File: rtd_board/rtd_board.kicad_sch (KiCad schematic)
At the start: 13 parts

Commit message: cleaning up
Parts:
- removed J?: Conn_02x18_Odd_Even, symbol Connector_Generic:Conn_02x18_Odd_Even
- removed J? (x2): Conn_01x15, symbol Connector_Generic:Conn_01x15
- removed U? (x9): MAX31865, symbol MAX31865:MAX31865
- removed U?: TCA9548A_Breakout, symbol TCA9548A_Breakout:TCA9548A_Breakout
- added J?: DSUB2, symbol Connector:DB15_Female
- added J?: DSUB3, symbol Connector:DB15_Female
- added J?: DSUB1, symbol Connector:DB15_Female
- added J?: Conn_02x18_Odd_Even, symbol Connector_Generic:Conn_02x18_Odd_Even
- added U? (x9): MAX31865, symbol MAX31865:MAX31865
- added U?: TCA9548A_Breakout, symbol TCA9548A_Breakout:TCA9548A_Breakout
- added U?: PCF8575_Breakout, symbol PCF8575_Breakout:PCF8575_Breakout
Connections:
- net +3V3: now also J?.1, J?.10 (P10), J?.12 (Pin_12), J?.4, U?. (VIN), U?.1 (V_IN), U?.1 (V_IN), U?.1 (V_IN), U?.1 (V_IN), U?.1 (V_IN), U?.1 (V_IN), U?.1 (V_IN), U?.1 (V_IN), U?.1 (V_IN)
- net FM1_INPT: now also J?.9 (P9)
- net FM2_INPT: now also J?.3
- net FM3_INPT: now also J?.12 (P12)
- net GND: now also J?.11 (P111), J?.2, J?.36 (Pin_36), J?.5, U?. (VIN), U?.7 (GND), U?.7 (GND), U?.7 (GND), U?.7 (GND), U?.7 (GND), U?.7 (GND), U?.7 (GND), U?.7 (GND), U?.7 (GND)
- net RTD1_CS: now also U?.5 (CS)
- net RTD1_SCK: now also U?.2 (SCK)
- net RTD1_SDI: now also U?.4 (SDI)
- net RTD1_SDO: now also U?.3 (SDO)
- new net MUX_SCL: J?.5 (Pin_5), U?. (VIN)
- new net MUX_SDA: J?.1 (Pin_1), U?. (VIN)
- new net RTD1_F+: J?.6, U?.9 (F+)
- new net RTD1_RTD+: J?.13 (P13), U?.11 (RTD+)
- new net RTD1_RTD-: J?.14 (P14), U?.12 (RTD-)
- new net RTD2_CS: U?.5 (CS)
- new net RTD2_F+: J?.15 (P15), U?.9 (F+)
- new net RTD2_RTD+: J?.7, U?.11 (RTD+)
- new net RTD2_RTD-: J?.8, U?.12 (RTD-)
- new net RTD2_SCK: U?.2 (SCK)
- new net RTD2_SDI: U?.4 (SDI)
- new net RTD3_CS: U?.5 (CS)
- new net RTD3_F+: J?.9 (P9), U?.9 (F+)
- new net RTD3_RTD+: J?.1, U?.11 (RTD+)
- new net RTD3_RTD-: J?.2, U?.12 (RTD-)
- new net RTD3_SCK: U?.2 (SCK)
- new net RTD3_SDI: U?.4 (SDI)
- new net RTD4_CS: U?.5 (CS)
- new net RTD4_F+: J?.3, U?.9 (F+)
- new net RTD4_RTD+: J?.10 (P10), U?.11 (RTD+)
- new net RTD4_RTD-: J?.11 (P111), U?.12 (RTD-)
- new net RTD4_SCK: U?.2 (SCK)
- new net RTD4_SDI: U?.4 (SDI)
- new net RTD4_SDO: U?.3 (SDO)
- new net RTD5_CS: U?.5 (CS)
- new net RTD5_F+: J?.12 (P12), U?.9 (F+)
- new net RTD5_RTD+: J?.4, U?.11 (RTD+)
- new net RTD5_RTD-: J?.14 (P14), J?.5, U?.12 (RTD-)
- new net RTD5_SCK: U?.2 (SCK)
- new net RTD5_SDI: U?.4 (SDI)
- new net RTD6_CS: U?.5 (CS)
- new net RTD6_F+: J?.6, U?.9 (F+)
- new net RTD6_RTD+: J?.13 (P13), U?.11 (RTD+)
- new net RTD6_RTD-: U?.12 (RTD-)
- new net RTD6_SCK: U?.2 (SCK)
- new net RTD6_SDI: U?.4 (SDI)
- new net RTD7_CS: U?.5 (CS)
- new net RTD7_F+: J?.15 (P15), U?.9 (F+)
- new net RTD7_RTD+: J?.7, U?.11 (RTD+)
- new net RTD7_RTD-: J?.8, U?.12 (RTD-)
- new net RTD7_SCK: U?.2 (SCK)
- new net RTD7_SDI: U?.4 (SDI)
- new net RTD7_SDO: U?.3 (SDO)
- new net RTD8_CS: U?.5 (CS)
- new net RTD8_F+: J?.9 (P9), U?.9 (F+)
- new net RTD8_RTD+: J?.1, U?.11 (RTD+)
- new net RTD8_RTD-: J?.2, U?.12 (RTD-), U?.12 (RTD-)
- new net RTD8_SCK: U?.2 (SCK)
- new net RTD8_SDI: U?.4 (SDI)
- new net RTD9_CS: U?.5 (CS)
- new net RTD9_F+: J?.3, U?.9 (F+)
- new net RTD9_RTD+: J?.10 (P10), U?.11 (RTD+)
- new net RTD9_RTD-: J?.11 (P111)
- new net RTD9_SCK: U?.2 (SCK)
- new net RTD9_SDI: U?.4 (SDI)
- no-connect marks 18 -> 27
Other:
- note added: "Address: 0x71"
- note added: "RTD 1"
- note added: "RTD 2"
- note added: "RTD 3"
- note added: "RTD 4"
- note added: "RTD 5"
- note added: "RTD 6"
- note added: "RTD 7"
- note added: "RTD 8"
- note added: "RTD 9"

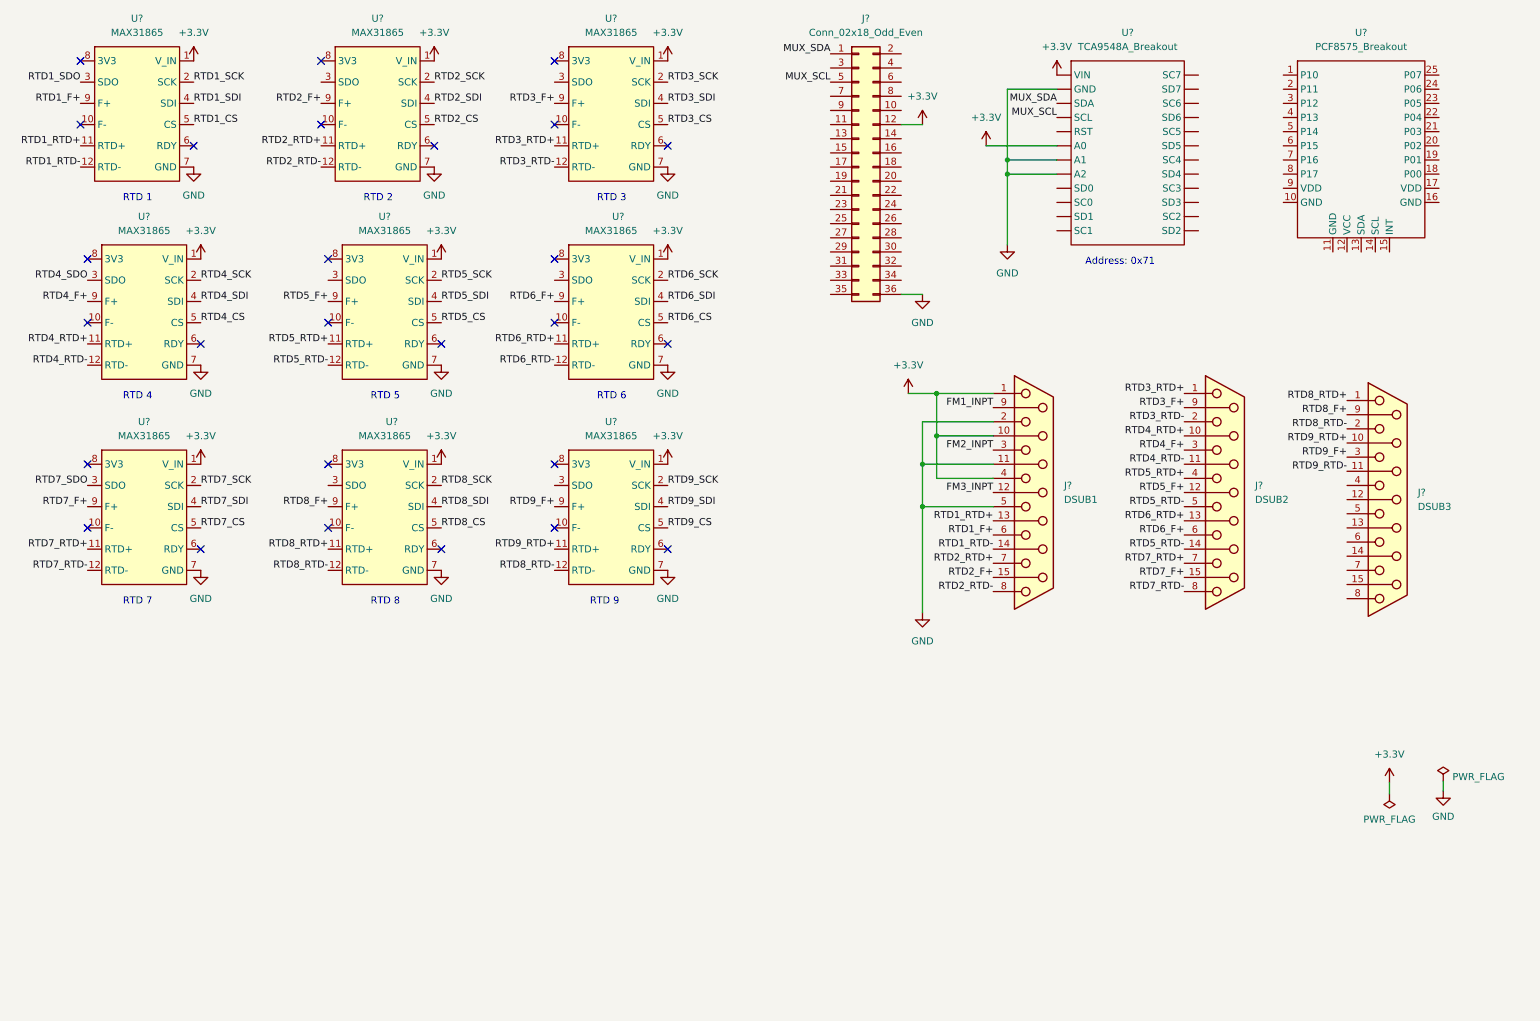
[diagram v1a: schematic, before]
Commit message: added screw terminals
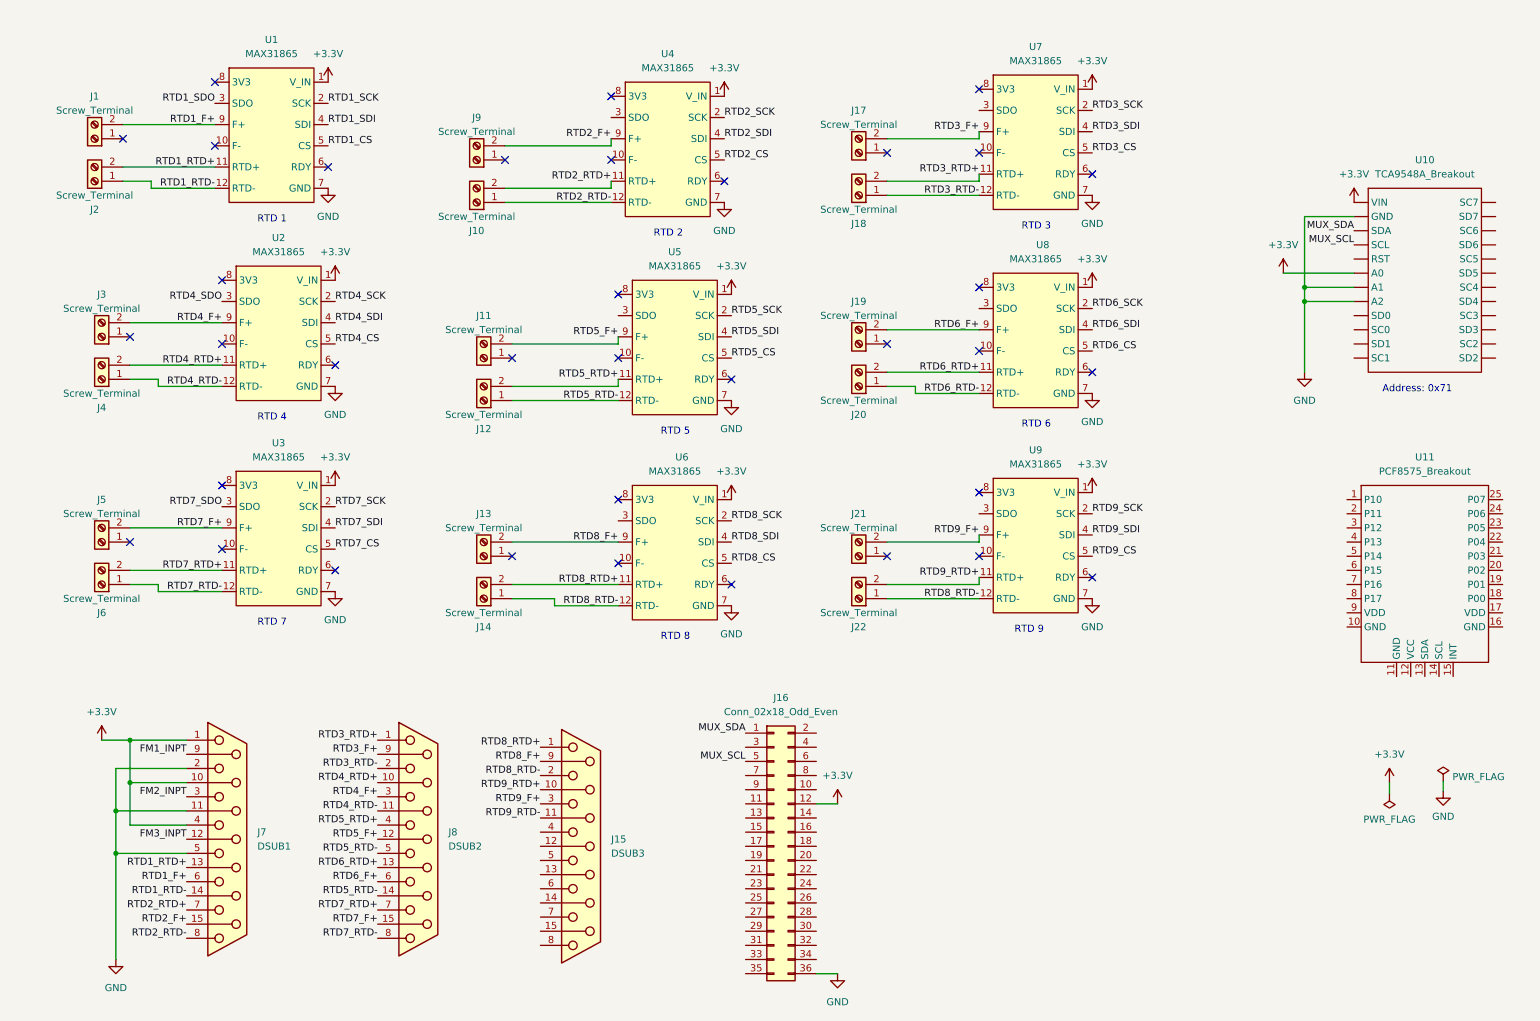
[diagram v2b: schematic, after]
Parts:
- added J1, J10, J11, J12, J13, J14, J17, J18, J19, J2, J20, J21, J22, J3, J4, J5, J6, J9: Screw_Terminal, symbol Connector:Screw_Terminal_01x02
- gave numbers to parts that had none: 15
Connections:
- net RTD1_F+: now also J1.2 (Pin_2)
- net RTD1_RTD+: now also J2.2 (Pin_2)
- net RTD1_RTD-: now also J2.1 (Pin_1)
- net RTD2_F+: now also J9.2 (Pin_2)
- net RTD2_RTD+: now also J10.2 (Pin_2)
- net RTD2_RTD-: now also J10.1 (Pin_1)
- net RTD3_F+: now also J17.2 (Pin_2)
- net RTD3_RTD+: now also J18.2 (Pin_2)
- net RTD3_RTD-: now also J18.1 (Pin_1)
- net RTD4_F+: now also J3.2 (Pin_2)
- net RTD4_RTD+: now also J4.2 (Pin_2)
- net RTD4_RTD-: now also J4.1 (Pin_1)
- net RTD5_F+: now also J11.2 (Pin_2)
- net RTD5_RTD+: now also J12.2 (Pin_2)
- net RTD5_RTD-: now also J12.1 (Pin_1)
- net RTD6_F+: now also J19.2 (Pin_2)
- net RTD6_RTD+: now also J20.2 (Pin_2)
- net RTD6_RTD-: now also J20.1 (Pin_1)
- net RTD7_F+: now also J5.2 (Pin_2)
- net RTD7_RTD+: now also J6.2 (Pin_2)
- net RTD7_RTD-: now also J6.1 (Pin_1)
- net RTD8_F+: now also J13.2 (Pin_2)
- net RTD8_RTD+: now also J14.2 (Pin_2)
- net RTD8_RTD-: now also J14.1 (Pin_1), J22.1 (Pin_1)
- net RTD9_F+: now also J21.2 (Pin_2)
- net RTD9_RTD+: now also J22.2 (Pin_2)
- no-connect marks 27 -> 36
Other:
- moved on the sheet: J15, J16, J7, J8, U1, U10, U11, U2, U3, U4, U5, U6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

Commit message: updates to layout + board settings, not complete yet
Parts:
- removed J1, J10, J11, J12, J13, J14, J17, J18, J19, J2, J20, J21, J22, J3, J4, J5, J6, J9: Screw_Terminal, symbol Connector:Screw_Terminal_01x02
- removed J15: DSUB3, symbol Connector:DB15_Female
- removed J16: Conn_02x18_Odd_Even, symbol Connector_Generic:Conn_02x18_Odd_Even
- removed U10: TCA9548A_Breakout, symbol TCA9548A_Breakout:TCA9548A_Breakout
- removed U11: PCF8575_Breakout, symbol PCF8575_Breakout:PCF8575_Breakout
- removed U9: MAX31865, symbol MAX31865:MAX31865
- added J1: PCIE-LP-01-01-F-DV-A-TR, Connector_PCBEdge:BUS_PCIexpress_x1, symbol PCIE-LP-01-01-F-DV-A-TR:PCIE-LP-01-01-F-DV-A-TR
- added U10: PCF8575_Breakout, PCF8575_Breakout:PCF8575_Breakout, symbol PCF8575_Breakout:PCF8575_Breakout
- J7, J8: footprint (none) -> DSUB_622-015-260-042:DSUB_622-015-260-042
- U1, U2, U3, U4, U5, U6, U7, U8: footprint (none) -> MAX31865_Breakout:MAX31865_Breakout
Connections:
- net FM1_INPT is gone; now on net RTD1_F+: J7.9 (P9)
- net FM2_INPT is gone; now on net RTD2_F+: J7.3
- net FM3_INPT is gone; now on net RTD3_F+: J7.12 (P12)
- net RTD1_SDO is gone; now on net SPI_MISO: U1.3 (SDO)
- net RTD2_SCK is gone; now on net SPI_SCK: U4.2 (SCK)
- net RTD2_SDI is gone; now on net SPI_MOSI: U4.4 (SDI)
- net RTD3_SCK is gone; now on net SPI_SCK: U7.2 (SCK)
- net RTD3_SDI is gone; now on net SPI_MOSI: U7.4 (SDI)
- net RTD4_SCK is gone; now on net SPI_SCK: U2.2 (SCK)
- net RTD4_SDI is gone; now on net SPI_MOSI: U2.4 (SDI)
- net RTD4_SDO is gone; now on net SPI_MISO: U2.3 (SDO)
- net RTD5_SCK is gone; now on net SPI_SCK: U5.2 (SCK)
- net RTD5_SDI is gone; now on net SPI_MOSI: U5.4 (SDI)
- net RTD6_SCK is gone; now on net SPI_SCK: U8.2 (SCK)
- net RTD6_SDI is gone; now on net SPI_MOSI: U8.4 (SDI)
- net RTD7_SCK is gone; now on net SPI_SCK: U3.2 (SCK)
- net RTD7_SDI is gone; now on net SPI_MOSI: U3.4 (SDI)
- net RTD7_SDO is gone; now on net SPI_MISO: U3.3 (SDO)
- net RTD8_SCK is gone; now on net SPI_SCK: U6.2 (SCK)
- net RTD8_SDI is gone; now on net SPI_MOSI: U6.4 (SDI)
- net GND: now also J1.A14, J1.A15, J1.B14, J1.B15, J1.B18, U10.10 (GND), U10.11 (GND), U10.16 (GND); no longer J7.11 (P111), J7.2, J7.5
- net RTD1_CS: now also U10.1 (P10)
- net RTD1_F+: no longer J7.6
- net RTD1_RTD+: now also J7.1; no longer J7.13 (P13)
- net RTD1_RTD-: now also J7.2; no longer J7.14 (P14)
- net RTD2_CS: now also U10.2 (P11)
- net RTD2_F+: no longer J7.15 (P15)
- net RTD2_RTD+: now also J7.10 (P10); no longer J7.7
- net RTD2_RTD-: now also J7.11 (P111); no longer J7.8
- net RTD3_CS: now also U10.3 (P12)
- net RTD3_F+: no longer J8.9 (P9)
- net RTD3_RTD+: now also J7.4; no longer J8.1
- net RTD3_RTD-: now also J7.5; no longer J8.2
- net RTD4_CS: now also U10.4 (P13)
- net RTD4_F+: now also J7.6; no longer J8.3
- net RTD4_RTD+: now also J7.13 (P13); no longer J8.10 (P10)
- net RTD4_RTD-: now also J7.14 (P14); no longer J8.11 (P111)
- net RTD5_CS: now also U10.5 (P14)
- net RTD5_F+: now also J7.15 (P15); no longer J8.12 (P12)
- net RTD5_RTD+: now also J7.7; no longer J8.4
- net RTD5_RTD-: now also J7.8; no longer J8.14 (P14), J8.5
- net RTD6_CS: now also U10.6 (P15)
- net RTD6_F+: now also J8.9 (P9); no longer J8.6
- net RTD6_RTD+: now also J8.1; no longer J8.13 (P13)
- net RTD6_RTD-: now also J8.2
- net RTD7_CS: now also U10.7 (P16)
- net RTD7_F+: now also J8.3; no longer J8.15 (P15)
- net RTD7_RTD+: now also J8.10 (P10); no longer J8.7
- net RTD7_RTD-: now also J8.11 (P111); no longer J8.8
- net RTD8_CS: now also U10.8 (P17)
- net RTD8_F+: now also J8.12 (P12)
- net RTD8_RTD+: now also J8.4
- net RTD8_RTD-: now also J8.5
- net SPI_MISO: now reaches U4.3 (SDO)
- net SPI_MISO: now also U5.3 (SDO), U6.3 (SDO), U7.3 (SDO), U8.3 (SDO), J1.A5
- net +3V3 renamed +3.3V
- net +3.3V: now also J1.A12, J1.A13, U10.12 (VCC), U10.17 (VDD), U10.9 (VDD); no longer J7.1, J7.10 (P10), J7.4
- net RTD1_SCK renamed SPI_SCK
- net SPI_SCK: now also J1.A7
- net RTD1_SDI renamed SPI_MOSI
- net SPI_MOSI: now also J1.A9
- new net IO_EXP_SC: J1.A3, U10.14 (SCL)
- new net IO_EXP_SD: J1.A1, U10.13 (SDA)
- no-connect marks 36 -> 63
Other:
- note removed: "Address: 0x71"
- note removed: "RTD 9"
- moved on the sheet: J7, J8, U4
